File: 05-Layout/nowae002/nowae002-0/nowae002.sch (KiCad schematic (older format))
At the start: 55 parts, among them P1 USB_A_90, Q1 IRLML6402, U2 TPS62152

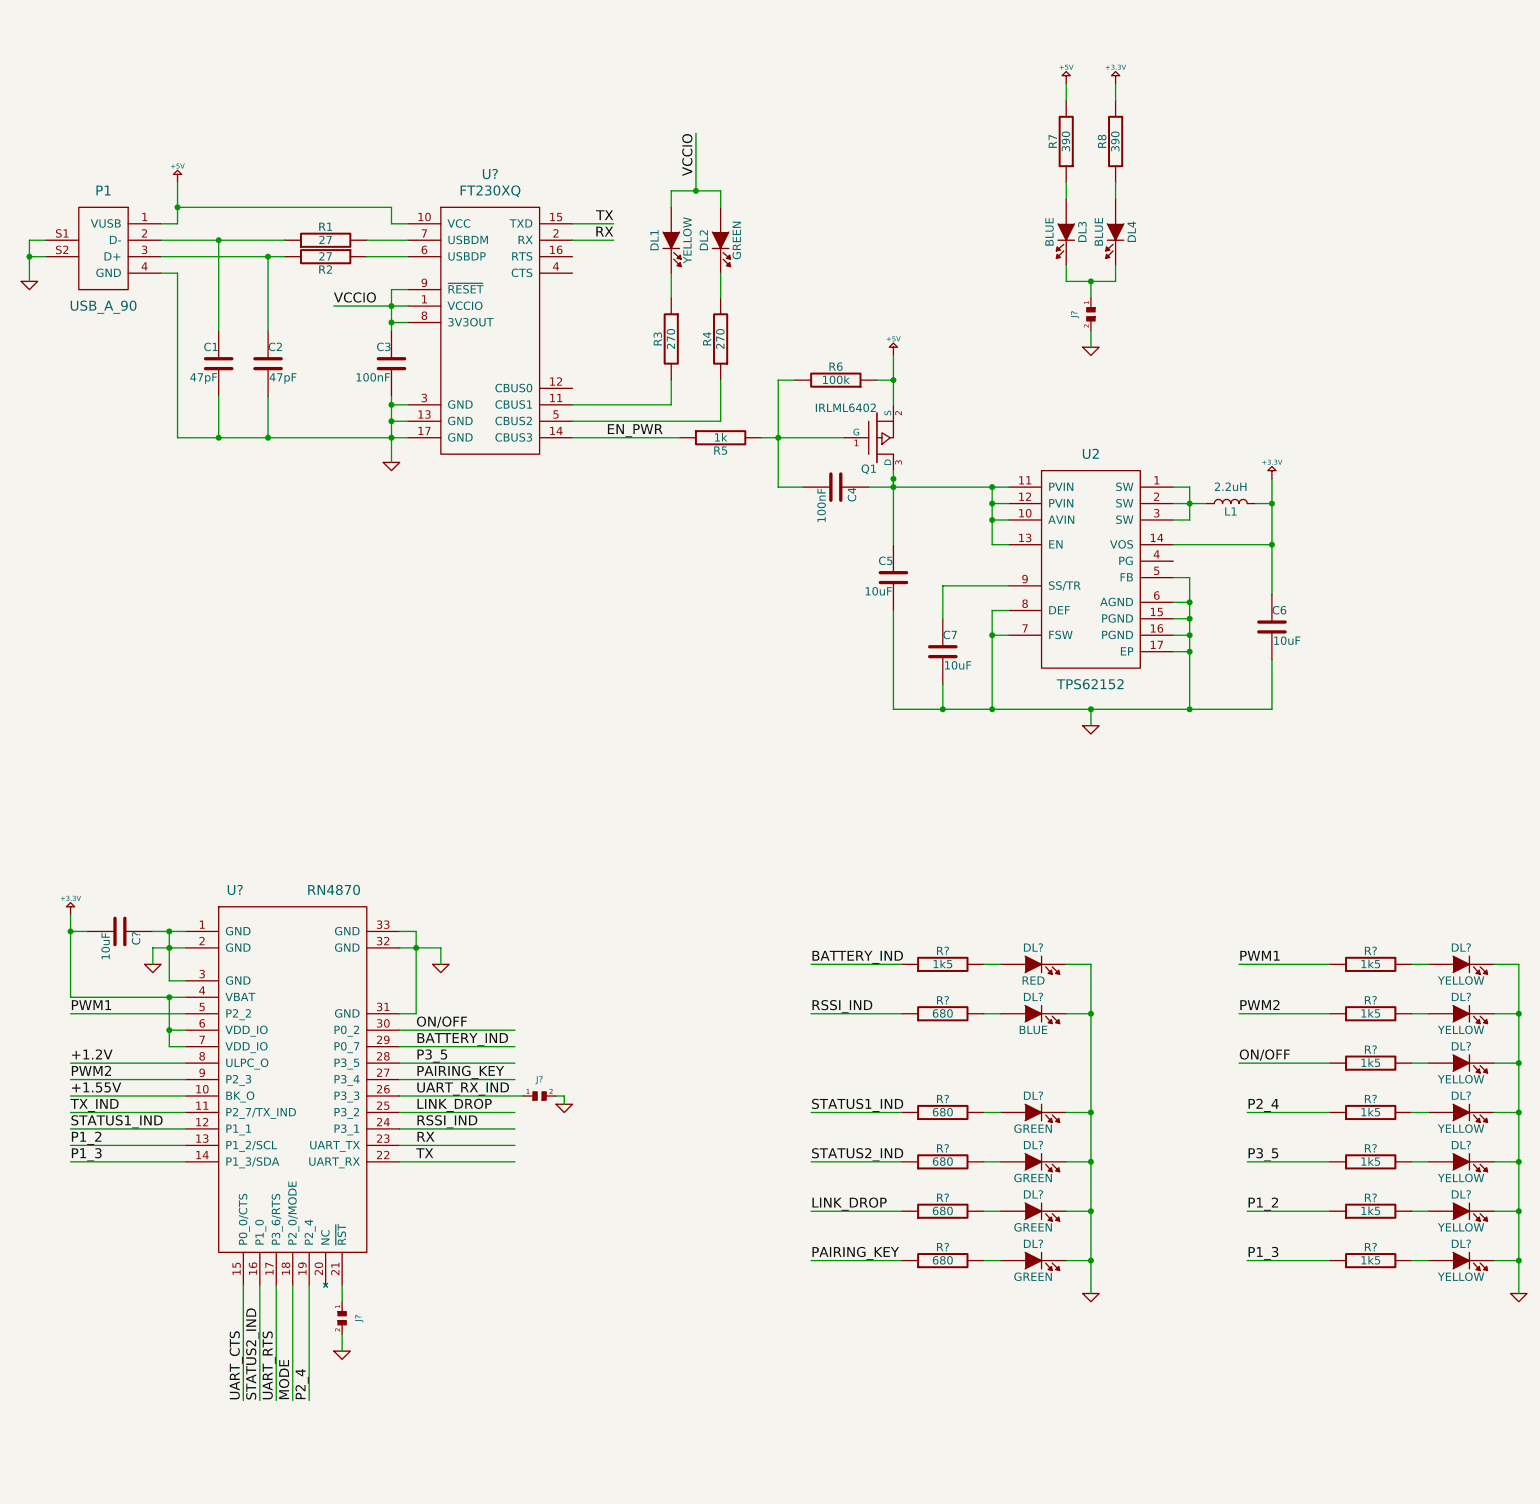
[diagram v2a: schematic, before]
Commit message: Annotated components in nowae002
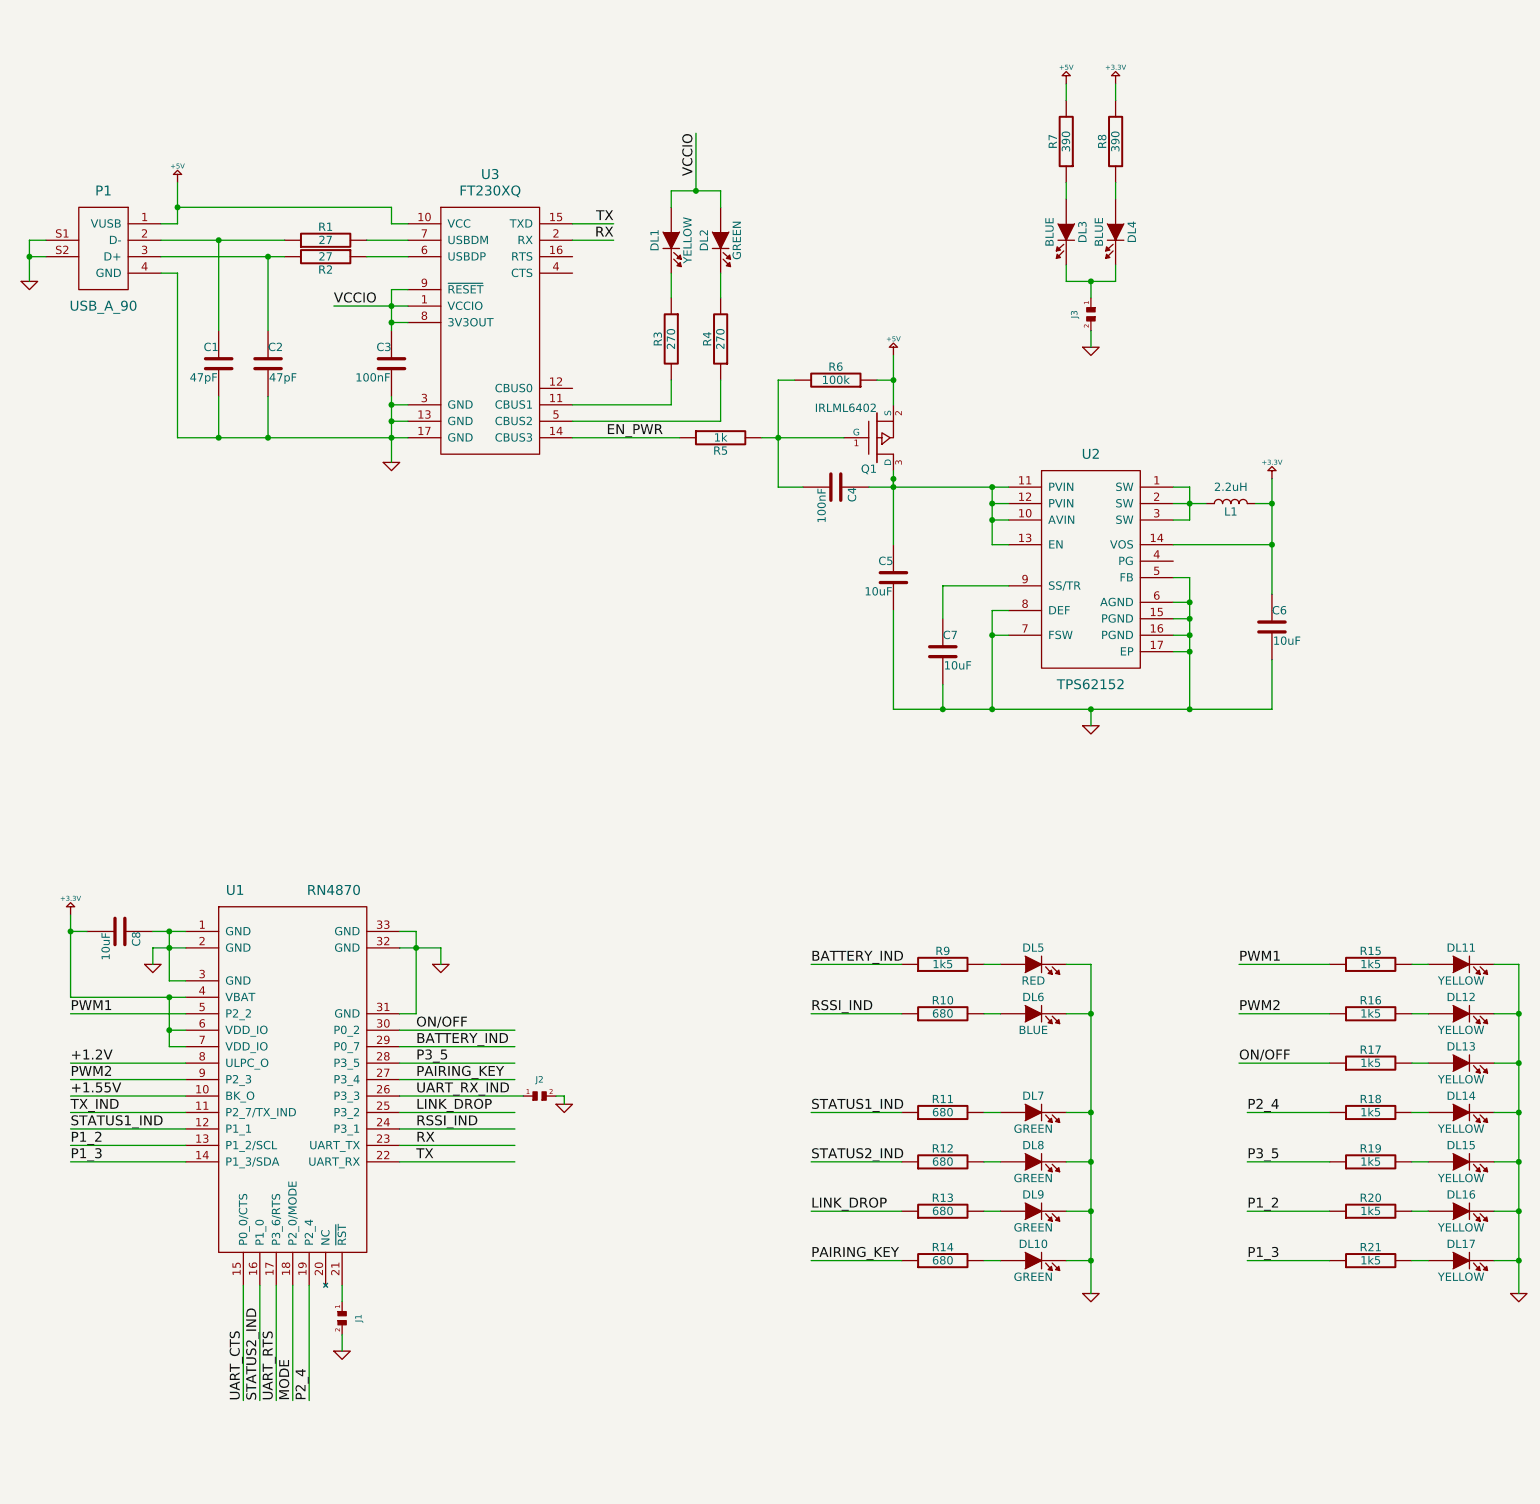
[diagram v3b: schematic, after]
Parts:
- gave numbers to parts that had none: 32

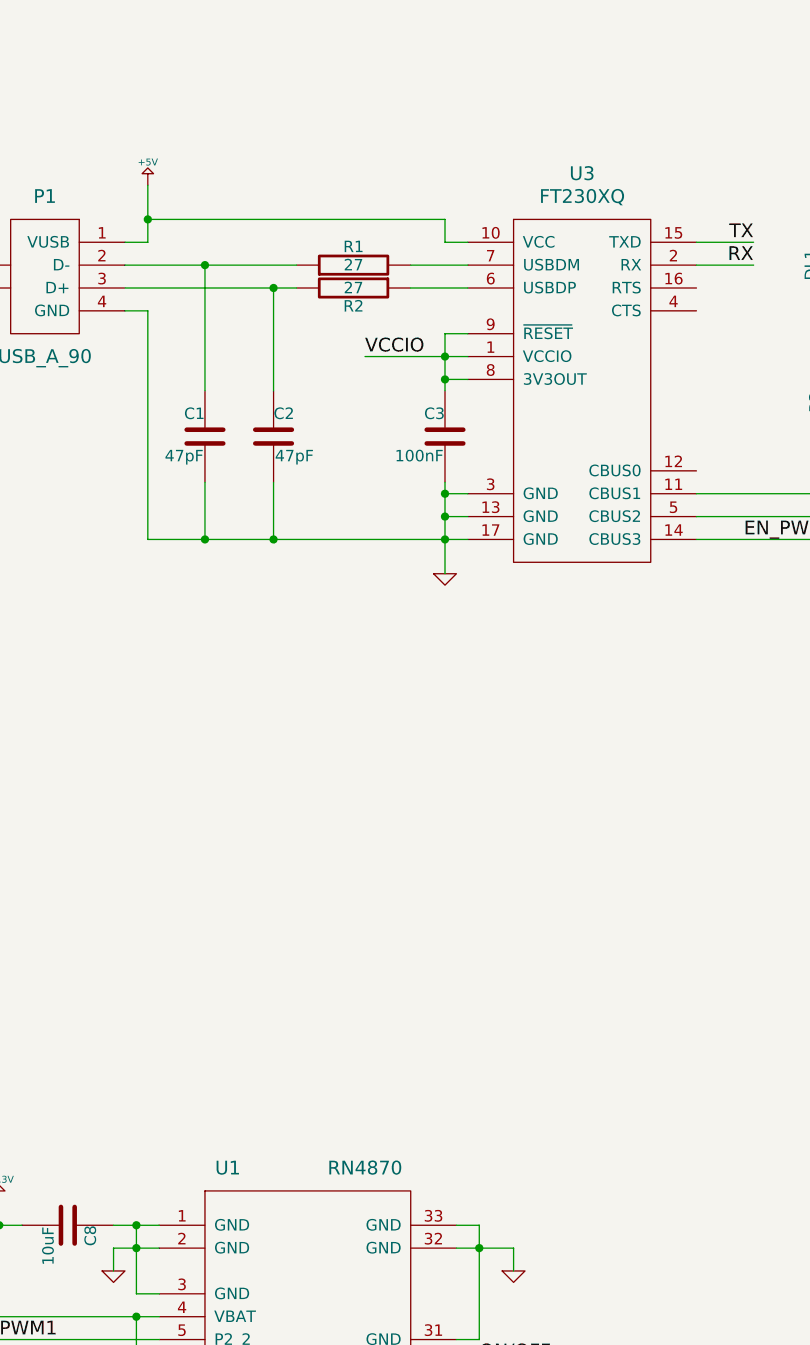
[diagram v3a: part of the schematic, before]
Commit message: Modified ref des in nowae002 (U3 -> U1)
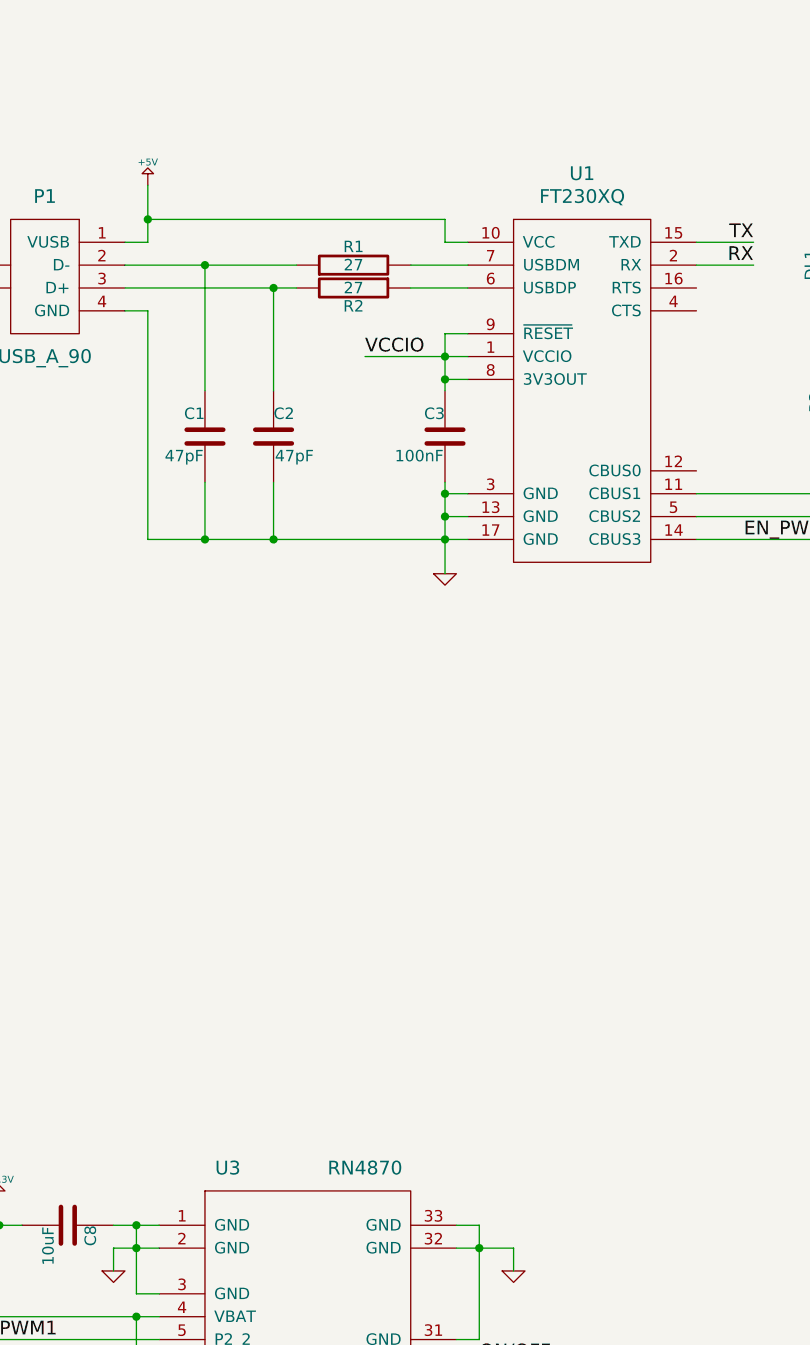
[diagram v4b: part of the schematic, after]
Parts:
- C1, C2, C3, C4, C5, C6, C7, C8: footprint (none) -> CAPACITOR:CAPACITOR-0402
- DL1, DL10, DL11, DL12, DL13, DL14, DL15, DL16, DL17, DL2, DL3, DL4, DL5, DL6, DL7, DL8, DL9: footprint (none) -> LEDs:LED-0402
- J1, J2, J3: footprint (none) -> MISC:JUMPERSMD-2
- L1: footprint (none) -> INDUCTOR:INDUCTOR-0805
- P1: footprint (none) -> CONNECTOR:USB-A-PLUG-SMD
- Q1: footprint (none) -> SOT:SOT23-3
- R1, R10, R11, R12, R13, R14, R15, R16, R17, R18, R19, R2, R20, R21, R3, R4, R5, R6, R7, R8, R9: footprint (none) -> RESISTOR:RESISTOR-0402
- U1: renamed from U3; footprint QFN16 -> QFN:QFN16_4x4_0.65_16+1
- U2: footprint VQFN16 -> QFN:QFN16_3x3_0.5_16+1
- U3: renamed from U1; footprint (none) -> WIFI:RN4870U
